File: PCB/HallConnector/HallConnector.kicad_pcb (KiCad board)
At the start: 2 copper layers, 21.5 x 19 mm, 19 parts, among them CN3 WAFER-SH1.0-4PWB, J1 Conn_01x05_Pin, U1 WAFER-SH1.0-2PWB, U2 WAFER-SH1.0-2PWB

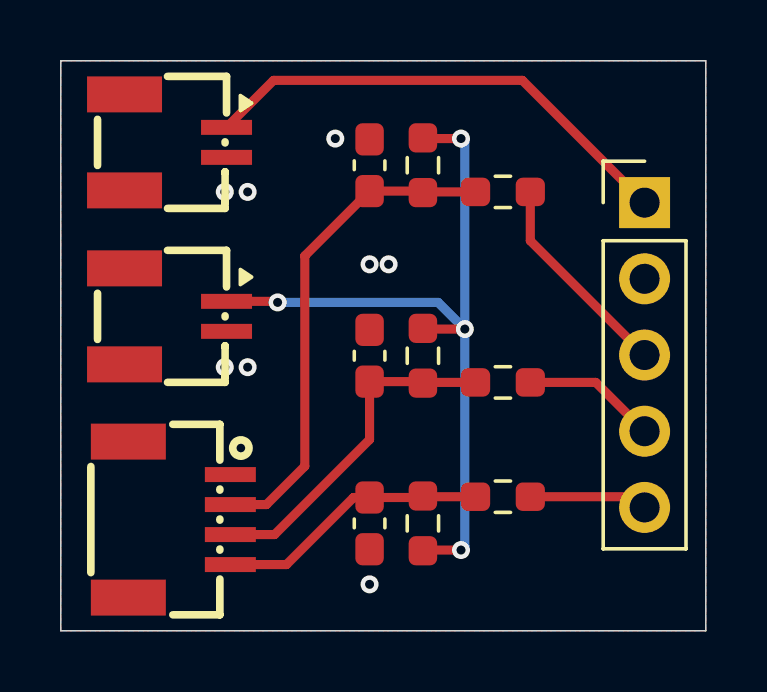
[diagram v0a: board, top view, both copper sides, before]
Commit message: 修复霍尔接口板线序问题，完成串口测试
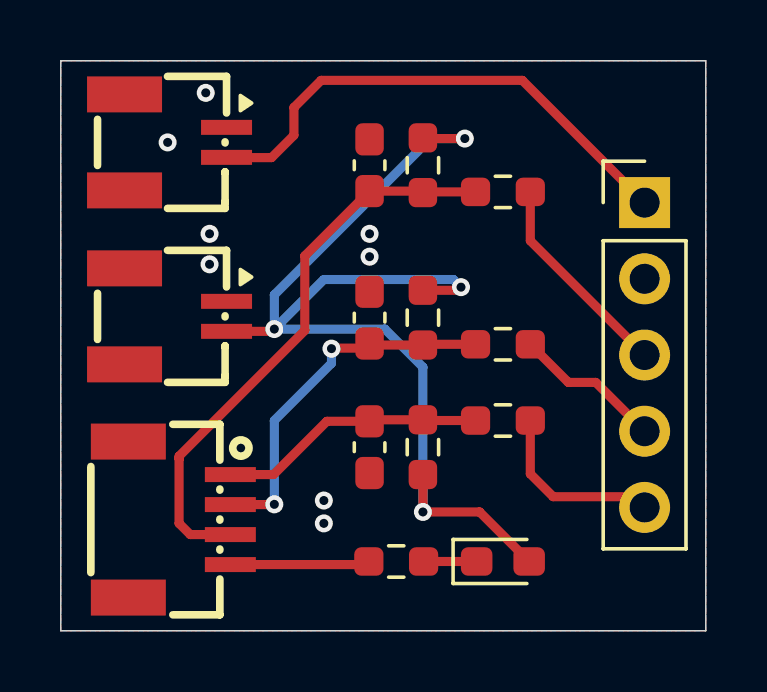
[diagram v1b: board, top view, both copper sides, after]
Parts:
- added D4: STA_LED, LED_SMD:LED_0603_1608Metric_Pad1.05x0.95mm_HandSolder, F.Cu at (134.2, 67.7)
- added R7: 510Ω, Resistor_SMD:R_0603_1608Metric_Pad0.98x0.95mm_HandSolder, F.Cu at (130.7, 67.7)
- moved C3 2.54 mm to (129.8, 63.9)
- moved R3 2.54 mm to (131.6, 63.9)
- moved R4 2.54 mm to (134.2, 63.0)
- moved R5 1.27 mm to (134.2, 60.5)
- moved C2 1.27 mm to (129.8, 59.6)
- moved R2 1.27 mm to (131.6, 59.6)
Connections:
- CN3 pad 1: unconnected-(CN3-Pad1) -> /SPI1_NSS
- CN3 pad 2: /SPI1_MISO -> /SPI1_MOSI
- CN3 pad 3: /SPI1_MOSI -> /SPI1_MISO
- CN3 pad 4: /SPI1_NSS -> /SPI1_SCK
- U1 pad 1: +3.3V -> GND
- U1 pad 2: GND -> +3.3V
- U2 pad 1: +5V -> GND
- U2 pad 2: GND -> +5V
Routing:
- net +3.3V: track 26.1 -> 36.7 mm
- net /SPI1_SCK: track 0.00 -> 4.51 mm
- net /SPI1_MISO: track 16.6 -> 19.0 mm
- net Net-(D4-K): track 0.00 -> 1.77 mm
- net Net-(J1-Pin_5): track 3.96 -> 5.55 mm
- net +5V: track 16.3 -> 17.2 mm
- net /SPI1_MOSI: track 11.4 -> 12.0 mm, vias 0 -> 2
- net Net-(J1-Pin_4): track 4.48 -> 5.01 mm

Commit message: 完成低端电流采样触发时间测试
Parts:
- removed kibuzzard-67F5322E: G***, kibuzzard-67F5322E
- removed kibuzzard-67F53345: G***, kibuzzard-67F53345
- removed kibuzzard-67F53375: G***, kibuzzard-67F53375
- removed kibuzzard-67F53F9F: G***, kibuzzard-67F53F9F
- removed kibuzzard-67F53FAD: G***, kibuzzard-67F53FAD
- removed kibuzzard-67F53FBB: G***, kibuzzard-67F53FBB
- added kibuzzard-67FE447B: G***, kibuzzard-67FE447B, B.Cu at (135.4, 55.8)
- added kibuzzard-67FE4499: G***, kibuzzard-67FE4499, B.Cu at (135.0, 58.3)
- added kibuzzard-67FE44A7: G***, kibuzzard-67FE44A7, B.Cu at (135.8, 60.9)
- added kibuzzard-67FE44AF: G***, kibuzzard-67FE44AF, B.Cu at (135.8, 63.5)
- added kibuzzard-67FE44BA: G***, kibuzzard-67FE44BA, B.Cu at (135.8, 66.0)
- added kibuzzard-67FE4510: G***, kibuzzard-67FE4510, B.Cu at (128.7, 60.5)
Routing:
- net Net-(J1-Pin_5): track 5.55 -> 5.01 mm
